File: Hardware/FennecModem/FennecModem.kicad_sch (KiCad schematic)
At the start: 0 parts

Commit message: Inital Docs
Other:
- added sheet ADC-DAC (cm108adc-dac.kicad_sch)
- added sheet Radio (radio.kicad_sch)
- company: (none) -> Kitsune Scientific
- title: (none) -> Fennec Modem
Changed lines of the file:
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@@
 (kicad_sch (version 20211123) (generator eeschema)
   (paper "A4")
+  (title_block
+    (title "Fennec Modem")
+    (date "${ISSUE}")
+    (rev "${REVISION}")
+    (company "Kitsune Scientific")
+    (comment 4 "${FULL_REVISION}")
+  )
   (symbol (lib_id "KenwoodFox:KITSUNE_LOGO") (at 278.13 175.895 0) (unit 1)
     (in_bom yes) (on_board yes) (fields_autoplaced)
-    (property "Reference" "#L?" (id 0) (at 278.13 171.6034 0)
+    (property "Reference" "#L101" (id 0) (at 278.13 171.6034 0)
       (effects (font (size 1.27 1.27)) hide)
     )
@@
     )
   )
+  (sheet (at 74.295 67.945) (size 31.115 57.15) (fields_autoplaced)
+    (stroke (width 0.1524) (type solid) (color 0 0 0 0))
+    (fill (color 0 0 0 0.0000))
+    (property "Sheet name" "ADC-DAC" (id 0) (at 74.295 67.2334 0)
+      (effects (font (size 1.27 1.27)) (justify left bottom))
+    )
+    (property "Sheet file" "cm108adc-dac.kicad_sch" (id 1) (at 74.295 125.6796 0)
+      (effects (font (size 1.27 1.27)) (justify left top))
+    )
+  )
+  (sheet (at 130.175 67.31) (size 32.385 58.42) (fields_autoplaced)
+    (stroke (width 0.1524) (type solid) (color 0 0 0 0))
+    (fill (color 0 0 0 0.0000))
+    (property "Sheet name" "Radio" (id 0) (at 130.175 66.5984 0)
+      (effects (font (size 1.27 1.27)) (justify left bottom))
+    )
+    (property "Sheet file" "radio.kicad_sch" (id 1) (at 130.175 126.3146 0)
+      (effects (font (size 1.27 1.27)) (justify left top))
+    )
+  )
   (sheet_instances
     (path "/" (page "1"))
+    (path "/cf3d0f33-271b-4df1-9d86-6d97bc01010a" (page "2"))
+    (path "/818ae4cb-50e5-4c8b-88f5-6f1511246083" (page "3"))
   )
   (symbol_instances
     (path "/94279616-57a4-4fdb-a78f-22414aa7050f"
-      (reference "#L?") (unit 1) (value "KITSUNE_LOGO") (footprint "")
+      (reference "#L101") (unit 1) (value "KITSUNE_LOGO") (footprint "")
+    )
+    (path "/cf3d0f33-271b-4df1-9d86-6d97bc01010a/5ed70f5a-9bfb-4732-b4b0-7d19d4f1f636"
+      (reference "#PWR0101") (unit 1) (value "+5V") (footprint "")
+    )
+    (path "/cf3d0f33-271b-4df1-9d86-6d97bc01010a/0166da6c-94ff-4d2b-8b5e-86a28e7bce28"
+      (reference "#PWR0102") (unit 1) (value "+5V") (footprint "")
+    )
+    (path "/cf3d0f33-271b-4df1-9d86-6d97bc01010a/a24a83ba-fd01-419f-8bbb-a66fea701abc"
+      (reference "#PWR0103") (unit 1) (value "GND") (footprint "")
+    )
+    (path "/cf3d0f33-271b-4df1-9d86-6d97bc01010a/46b1ab82-9a02-4f59-b80e-ef33dbe56a9b"
+      (reference "#PWR0104") (unit 1) (value "+5V") (footprint "")
+    )
+    (path "/cf3d0f33-271b-4df1-9d86-6d97bc01010a/d6520202-0ebe-4a20-b4dd-d2df890fa3ef"
+      (reference "#PWR0105") (unit 1) (value "+5V") (footprint "")
+    )
+    (path "/cf3d0f33-271b-4df1-9d86-6d97bc01010a/88d4e7aa-99e2-4daa-8fe5-7cd5f0ed8364"
+      (reference "#PWR0106") (unit 1) (value "GND") (footprint "")
+    )
+    (path "/cf3d0f33-271b-4df1-9d86-6d97bc01010a/35c8f909-8923-486e-b8aa-51da59e97d87"
+      (reference "#PWR0107") (unit 1) (value "GND") (footprint "")
+    )
+    (path "/cf3d0f33-271b-4df1-9d86-6d97bc01010a/304c923a-36e8-48d0-8ef5-04dbbe1da7c2"
+      (reference "#PWR0108") (unit 1) (value "GND") (footprint "")
+    )
+    (path "/cf3d0f33-271b-4df1-9d86-6d97bc01010a/ee0322de-c76a-42ad-a3f7-11522c74d0b4"
+      (reference "#PWR0109") (unit 1) (value "GND") (footprint "")
+    )
+    (path "/cf3d0f33-271b-4df1-9d86-6d97bc01010a/0df8b3bd-b6f1-4186-bb72-8bb79345596e"
+      (reference "#PWR?") (unit 1) (value "+5V") (footprint "")
+    )
+    (path "/cf3d0f33-271b-4df1-9d86-6d97bc01010a/165374fd-7e76-4f05-b8cb-47c94e7d8ffe"
+      (reference "#PWR?") (unit 1) (value "GND") (footprint "")
+    )
+    (path "/cf3d0f33-271b-4df1-9d86-6d97bc01010a/1f09fd58-bfa4-47f8-80eb-35167f865270"
+      (reference "#PWR?") (unit 1) (value "GND") (footprint "")
+    )
+    (path "/cf3d0f33-271b-4df1-9d86-6d97bc01010a/8fe6670a-65d4-4163-890a-8da69d672cc6"
+      (reference "C201") (unit 1) (value "4.7μf") (footprint "Capacitor_SMD:C_0805_2012Metric")
+    )
+    (path "/cf3d0f33-271b-4df1-9d86-6d97bc01010a/e3510515-5063-4344-b3f9-730e896be801"
+      (reference "C202") (unit 1) (value "0.1μf") (footprint "Capacitor_SMD:C_0805_2012Metric")
+    )
+    (path "/cf3d0f33-271b-4df1-9d86-6d97bc01010a/ddfbd8c2-6aac-4979-aa9d-3d1c6bf0d369"
+      (reference "D?") (unit 1) (value "RX") (footprint "LED_SMD:LED_0603_1608Metric")
+    )
+    (path "/cf3d0f33-271b-4df1-9d86-6d97bc01010a/fe83e7fb-0b95-44ab-818b-1756453b8ab6"
+      (reference "D?") (unit 1) (value "TX") (footprint "LED_SMD:LED_0603_1608Metric")
+    )
+    (path "/cf3d0f33-271b-4df1-9d86-6d97bc01010a/f3cf3aac-2333-4ed9-8be9-562f2a4c4074"
+      (reference "FL201") (unit 1) (value "LFCN-490") (footprint "Filter:Filter_Mini-Circuits_FV1206")
+    )
+    (path "/cf3d0f33-271b-4df1-9d86-6d97bc01010a/eb263348-7250-40db-b9e3-039ac76d6930"
+      (reference "J201") (unit 1) (value "Conn_Coaxial") (footprint "Connector_Coaxial:SMA_Amphenol_132289_EdgeMount")
+    )
+    (path "/cf3d0f33-271b-4df1-9d86-6d97bc01010a/717c7c6f-9f9a-4dcb-9324-e20a77949e93"
+      (reference "JP201") (unit 1) (value "H/L Jumper") (footprint "Connector_PinHeader_2.54mm:PinHeader_1x02_P2.54mm_Vertical")
+    )
+    (path "/cf3d0f33-271b-4df1-9d86-6d97bc01010a/1e3d92e0-cb4a-4950-bb4c-d1af0a08a3db"
+      (reference "R201") (unit 1) (value "10k") (footprint "Resistor_SMD:R_0805_2012Metric")
+    )
+    (path "/cf3d0f33-271b-4df1-9d86-6d97bc01010a/391c5615-b4de-4570-8916-7eac28667399"
+      (reference "R?") (unit 1) (value "180") (footprint "Resistor_SMD:R_0805_2012Metric")
+    )
+    (path "/cf3d0f33-271b-4df1-9d86-6d97bc01010a/ad59940b-8504-44eb-8ecc-bcbbc8ae82e8"
+      (reference "R?") (unit 1) (value "47R") (footprint "Resistor_SMD:R_0805_2012Metric")
+    )
+    (path "/cf3d0f33-271b-4df1-9d86-6d97bc01010a/e60948b3-af21-4763-acf7-24df2d399918"
+      (reference "R?") (unit 1) (value "180") (footprint "Resistor_SMD:R_0805_2012Metric")
+    )
+    (path "/cf3d0f33-271b-4df1-9d86-6d97bc01010a/fb24d8dc-2ffd-4d7d-b9eb-a6628c5a70c8"
+      (reference "U201") (unit 1) (value "DRA818V") (footprint "KenwoodFox:DRA818V")
     )
   )

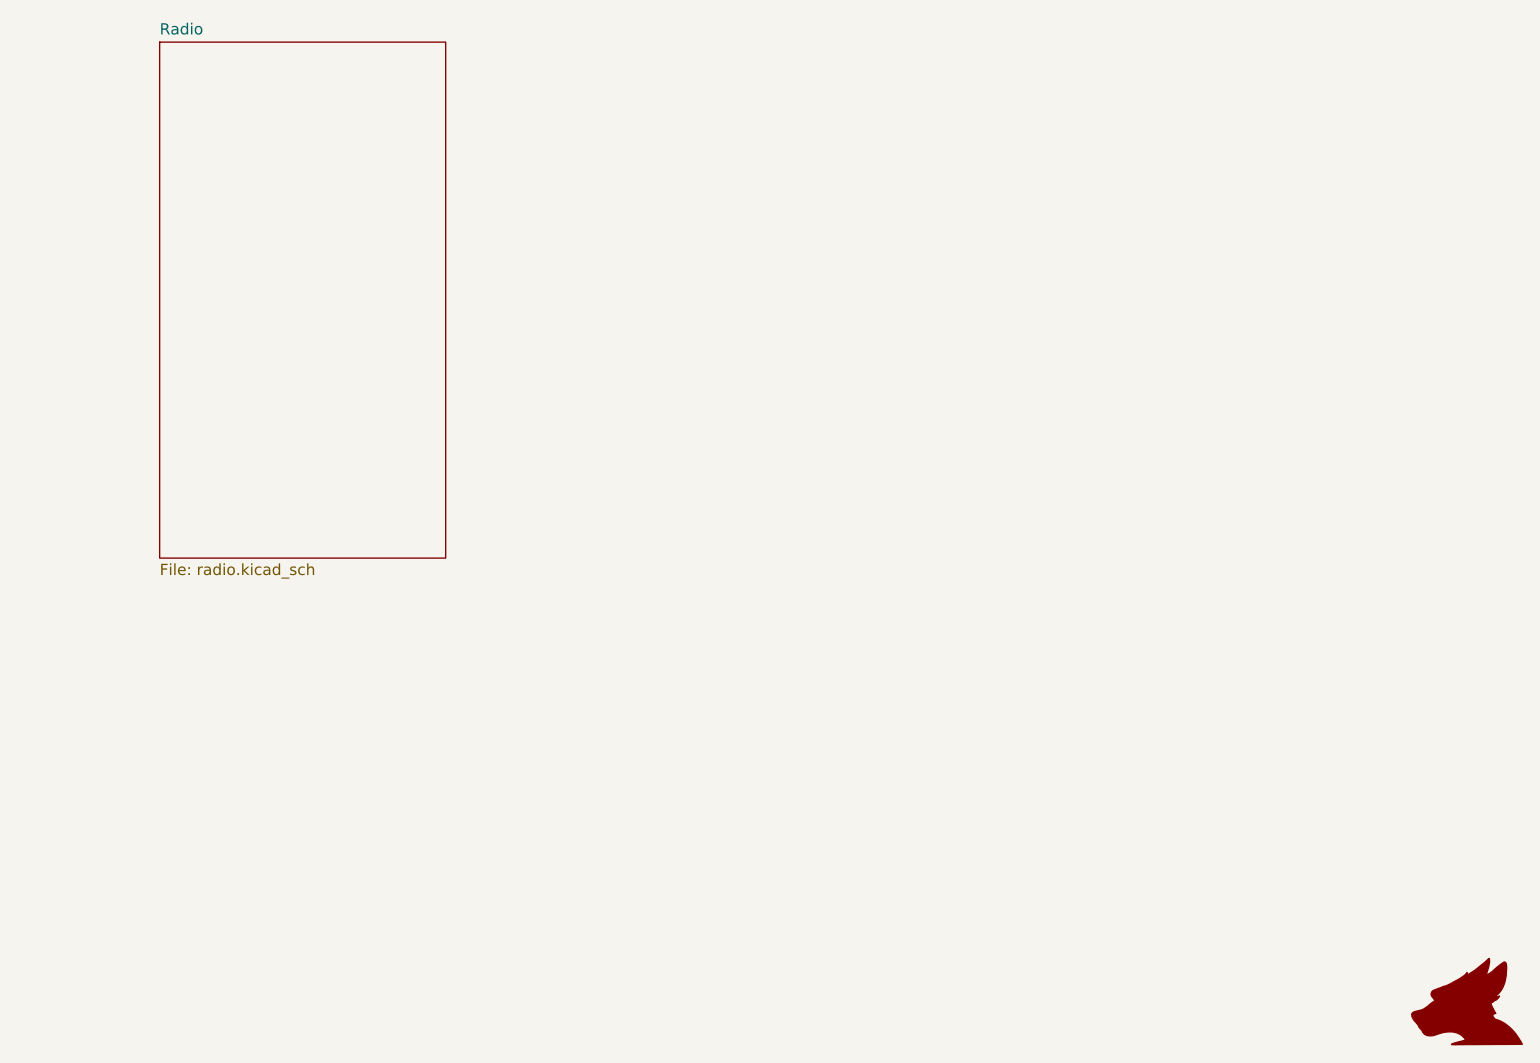
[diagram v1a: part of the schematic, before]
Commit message: Add modem components, bump edge card connector in upstream
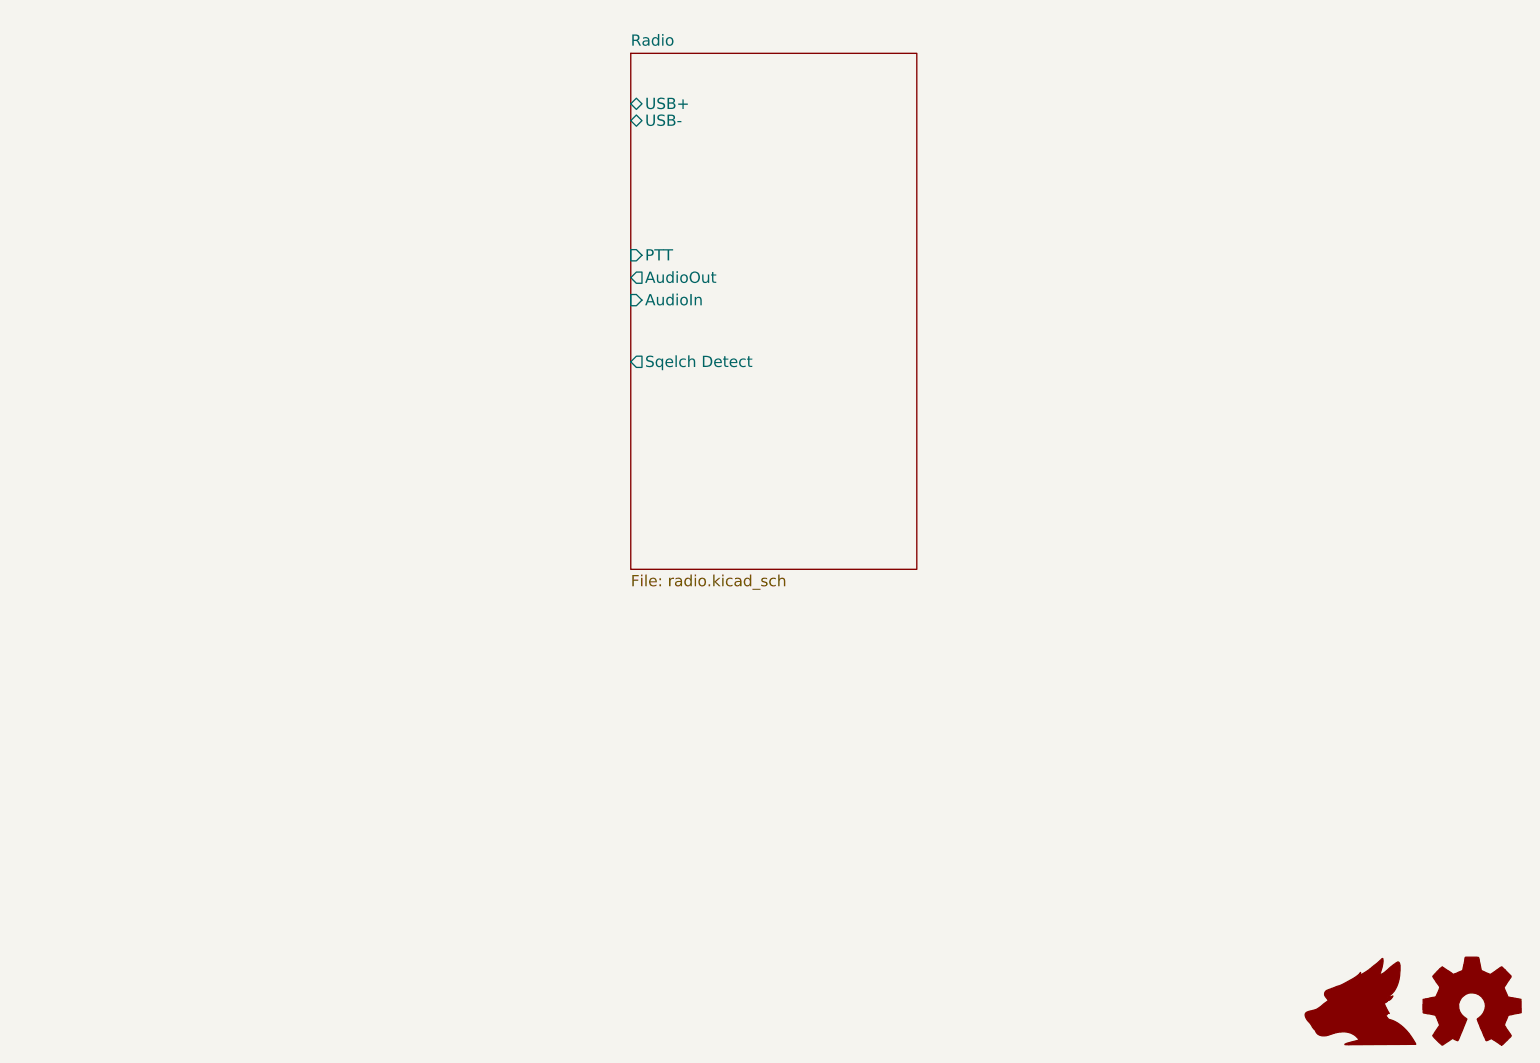
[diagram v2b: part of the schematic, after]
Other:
- sheet Radio ports: added AudioIn, AudioOut, PTT, Sqelch Detect, USB+, USB-; removed none

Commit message: F*ck yeah edge connectors!
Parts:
- added C101: EBM15DSEH, symbol KenwoodFox:EBM15DSEH
- added J101: USB_C_Receptacle_USB2.0, Connector_USB:USB_C_Receptacle_Palconn_UTC16-G, symbol Connector:USB_C_Receptacle_USB2.0
- added U101: ATmega32U4-A, Package_QFP:TQFP-44_10x10mm_P0.8mm, symbol MCU_Microchip_ATmega:ATmega32U4-A
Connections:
- new net: U101.14 (VCC), U101.34 (VCC)
- new net: U101.24 (AVCC), U101.44 (AVCC)
- new net: J101.A4 (VBUS), J101.A9 (VBUS), J101.B4 (VBUS), J101.B9 (VBUS)
- new net GND: J101.A1 (GND), J101.A12 (GND), J101.B1 (GND), J101.B12 (GND), J101.S1 (SHIELD), U101.15 (GND), U101.23 (GND), U101.35 (GND), U101.43 (GND), U101.5 (UGND)
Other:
- removed sheet ADC-DAC

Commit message: Add more
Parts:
- C101: footprint (none) -> KenwoodFox:Lewis_Card_Connector
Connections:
- net GND: now also C101.15, C101.30
- net +5V: now reaches C101.1
- net +12V: now reaches C101.16
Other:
- sheet Radio ports: added RXD, TXD; removed USB+, USB-

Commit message: Inital Backplane (#1)
Inital backplane is done, another PR can be opened later for more advanced stuff.
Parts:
- removed C101: EBM15DSEH, KenwoodFox:Lewis_Card_Connector, symbol KenwoodFox:EBM15DSEH
- added C102, C103: 22pf, Capacitor_SMD:C_0603_1608Metric, symbol Device:C_Small
- added C104: 100nf, Capacitor_SMD:C_0805_2012Metric, symbol Device:C_Small
- added C105: 1uf, Capacitor_SMD:C_0805_2012Metric, symbol Device:C_Small
- added D105: MBR0520LT, Diode_SMD:D_SOD-123, symbol Diode:MBR0520LT
- added D201: STAT, LED_THT:LED_D3.0mm_Horizontal_O1.27mm_Z2.0mm, symbol Device:LED
- added D201: SCK, LED_SMD:LED_0805_2012Metric, symbol Device:LED
- added D201: PWR, LED_THT:LED_D3.0mm_Horizontal_O1.27mm_Z2.0mm, symbol Device:LED
- added D6: PRTR5V0U2X, Package_TO_SOT_SMD:SOT-143, symbol Power_Protection:PRTR5V0U2X
- added J102: ICSP, Connector:Tag-Connect_TC2030-IDC-FP_2x03_P1.27mm_Vertical, symbol Connector_Generic:Conn_02x03_Odd_Even
- added R104, R105: 5K1, Resistor_SMD:R_0805_2012Metric, symbol Device:R_Small
- added R202 (x3): 330, Resistor_SMD:R_0805_2012Metric, symbol Device:R
- added R205: 10K, Resistor_SMD:R_0805_2012Metric, symbol Device:R
- added R205 (x2): 22R, Resistor_SMD:R_0805_2012Metric, symbol Device:R
- added SW101: RESET, Button_Switch_THT:SW_PUSH_6mm_H5mm, symbol Switch:SW_Push
- added Y101: 16mHz, Crystal:Crystal_SMD_HC49-SD, symbol Device:Crystal
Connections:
- net +5V: now also U101.14 (VCC), U101.2 (UVCC), U101.24 (AVCC), U101.34 (VCC), U101.44 (AVCC), D6.4 (VCC), J102.2 (Pin_2), R202.2, R202.2, R205.1
- net GND: now also C102.2, C103.2, C104.2, C105.2, D201.1 (K), D201.1 (K), D6.1 (GND), J102.6 (Pin_6), R104.1, R105.1, SW101.2
- net SDO: now reaches U101.10 (PB2)
- net SDO: now also J102.4 (Pin_4)
- net SDI: now reaches U101.11 (PB3)
- net SDI: now also J102.1 (Pin_1)
- net RESET: now reaches U101.13 (~{RESET})
- net RESET: now also J102.5 (Pin_5), R205.2, SW101.1
- net at U101.16 (XTAL2): now also C103.1, Y101.1
- net at U101.17 (XTAL1): now also C102.1, Y101.2
- net I2C_CLK: now reaches U101.18 (PD0)
- net I2C_SDA: now reaches U101.19 (PD1)
- net RXD: now reaches U101.20 (PD2)
- net TXD: now reaches U101.21 (PD3)
- net at U101.3 (D-): now also R205.1
- net TX_SIGNAL: now reaches U101.30 (PB6)
- net at U101.4 (D+): now also R205.1
- net RX_SIGNAL: now reaches U101.41 (PF0)
- net AREF: now reaches U101.42 (AREF)
- net AREF: now also C104.1
- net at U101.6 (UCAP): now also C105.1
- net SCK: now reaches U101.9 (PB1)
- net SCK: now also J102.3 (Pin_3), R202.2
- net at J101.A4 (VBUS), J101.A9 (VBUS), J101.B4 (VBUS)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: now also D105.2 (A)
- net at J101.A5 (CC1): now also R105.2
- net USB+: now reaches J101.A6 (D+)
- net USB+: now also J101.B6 (D+), D6.2 (I/O1), R205.2
- net USB-: now reaches J101.A7 (D-)
- net USB-: now also J101.B7 (D-), D6.3 (I/O2), R205.2
- net at J101.B5 (CC2): now also R104.2
- new net: D201.2 (A), R202.1 (x3)
- new net STAT: D201.1 (K)
- no-connect marks 0 -> 2
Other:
- added sheet Backplane (Backplane.kicad_sch)
- sheet Radio ports: added H/L, SQL, Sleep; removed Sqelch Detect
- note added: "Human Interface"
- note added: "ICSP"
- note added: "PB6/ADC13 Should be able to handle 16bit pwm"
- note added: "PF0 or A5 is ADC0"
- moved on the sheet: J101, U101

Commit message: Tones (#2)
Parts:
- removed C102, C103: 22pf, Capacitor_SMD:C_0603_1608Metric, symbol Device:C_Small
- removed C104: 100nf, Capacitor_SMD:C_0805_2012Metric, symbol Device:C_Small
- removed C105: 1uf, Capacitor_SMD:C_0805_2012Metric, symbol Device:C_Small
- removed D105: MBR0520LT, Diode_SMD:D_SOD-123, symbol Diode:MBR0520LT
- removed D201: SCK, LED_SMD:LED_0805_2012Metric, symbol Device:LED
- removed D6: PRTR5V0U2X, Package_TO_SOT_SMD:SOT-143, symbol Power_Protection:PRTR5V0U2X
- removed J101: USB_C_Receptacle_USB2.0, Connector_USB:USB_C_Receptacle_Palconn_UTC16-G, symbol Connector:USB_C_Receptacle_USB2.0
- removed J102: ICSP, Connector:Tag-Connect_TC2030-IDC-FP_2x03_P1.27mm_Vertical, symbol Connector_Generic:Conn_02x03_Odd_Even
- removed R104, R105: 5K1, Resistor_SMD:R_0805_2012Metric, symbol Device:R_Small
- removed R202: 330, Resistor_SMD:R_0805_2012Metric, symbol Device:R
- removed R205: 10K, Resistor_SMD:R_0805_2012Metric, symbol Device:R
- removed R205 (x2): 22R, Resistor_SMD:R_0805_2012Metric, symbol Device:R
- removed SW101: RESET, Button_Switch_THT:SW_PUSH_6mm_H5mm, symbol Switch:SW_Push
- removed U101: ATmega32U4-A, Package_QFP:TQFP-44_10x10mm_P0.8mm, symbol MCU_Microchip_ATmega:ATmega32U4-A
- removed Y101: 16mHz, Crystal:Crystal_SMD_HC49-SD, symbol Device:Crystal
- added A1: RaspberryPi_Pico, Module:RaspberryPi_Pico_Common_THT, symbol MCU_Module:RaspberryPi_Pico
- added C1: 1μf, Capacitor_SMD:C_0805_2012Metric, symbol Device:C_Small
- added M1: Fan, Connector_JST:JST_EH_B2B-EH-A_1x02_P2.50mm_Vertical, symbol Motor:Fan
- added Q3: MMBT3906, Package_TO_SOT_SMD:SOT-23, symbol Transistor_BJT:MMBT3906
- added R9: 10k, Resistor_SMD:R_0805_2012Metric, symbol Device:R_Small
- renumbered D201 to D101, D201 to D104, R202 to R103, R202 to R108
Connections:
- net +5V: now also A1.39 (VSYS), C1.1, M1.1 (+); no longer R103.2, R108.2
- net GND: now also D101.1 (K), A1.13 (GND), A1.18 (GND), A1.23 (GND), A1.28 (GND), A1.3 (GND), A1.38 (GND), A1.8 (GND), Q3.3 (C)
- net RXD: now also A1.11 (GPIO8)
- net SDI: now also A1.25 (GPIO19)
- net SDO: now also A1.21 (GPIO16)
- net STAT: now also R103.2, A1.9 (GPIO6); no longer D101.1 (K)
- net TXD: now also A1.12 (GPIO9)
- new net: C1.2, M1.2 (-), Q3.2 (E)
- new net: Q3.1 (B), R9.1
- new net +3.3V: A1.36 (3V3), R108.2
- new net CARD_SEL: A1.22 (GPIO17)
- new net FAN: A1.34 (GPIO28_ADC2), R9.2
- new net GNDA: A1.33 (AGND)
- new net H/L: A1.16 (GPIO12)
- new net PTT: A1.14 (GPIO10)
- new net SCL: A1.7 (GPIO5)
- new net SDA: A1.6 (GPIO4)
- new net SPI2: A1.26 (GPIO20)
- new net SPI3: A1.27 (GPIO21)
- new net SPI4: A1.29 (GPIO22)
- new net SPI_CLK: A1.24 (GPIO18)
- new net SQL: A1.17 (GPIO13)
- new net Sleep: A1.15 (GPIO11)
- new net TONE_IN: A1.31 (GPIO26_ADC0)
- new net TONE_OUT: A1.4 (GPIO2)
- no-connect marks 2 -> 11
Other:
- added sheet Audio Processing (Audio Processing.kicad_sch)
- sheet Backplane ports: added CARD_SEL, SPI_CLK, SPI_SDA1, SPI_SDA2, SPI_SDA3, SPI_SDA4, SPI_SDO; removed none
- note added: "Reccomended to prevent noise on RX"
- note removed: "ICSP"
- note removed: "PB6/ADC13 Should be able to handle 16bit pwm"
- note removed: "PF0 or A5 is ADC0"
- moved on the sheet: D101, R103
